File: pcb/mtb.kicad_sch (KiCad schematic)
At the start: 50 parts, among them J4 PINHEADER, J5 PROG/DEBUG, J6 PINHEADER, SW1 6x6, U12 STM32F103C8Tx, U13 AMS1117-3.3, U14 L78L05_SOT89, U15 SN75176AP, Y1 14,7456MHz

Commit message: Added Schottky in DCC part and fuse footprint.
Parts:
- F3: footprint (none) -> Fuse:Fuse_1812_4532Metric_Pad1.30x3.40mm_HandSolder
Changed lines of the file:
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@@
       (effects (font (size 1.27 1.27)))
     )
-    (property "Footprint" "" (at 265.43 26.67 0)
+    (property "Footprint" "Fuse:Fuse_1812_4532Metric_Pad1.30x3.40mm_HandSolder" (at 265.43 26.67 0)
       (effects (font (size 1.27 1.27)) (justify left) hide)
     )

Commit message: Add several notes.
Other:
- note added: "10k/each"
- moved on the sheet: D4, D5, D6, R39, R41, R42, SW1

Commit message: PCB WIP.
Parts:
- renumbered J4 to J7, J5 to J8
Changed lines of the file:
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@@
   (symbol (lib_id "Connector_Generic:Conn_02x05_Odd_Even") (at 74.93 176.53 0) (unit 1)
     (in_bom yes) (on_board yes) (dnp no)
-    (property "Reference" "J5" (at 76.2 165.9382 0)
+    (property "Reference" "J8" (at 76.2 165.9382 0)
       (effects (font (size 1.27 1.27)))
     )
@@
       (project "railcomdet"
         (path "/3e59d29f-2657-4552-9290-3c54fadfdf63/c65c8567-2dc1-4e1e-ba1a-da7bb38dcfe3"
-          (reference "J5") (unit 1)
+          (reference "J8") (unit 1)
         )
       )
@@
   (symbol (lib_id "Connector_Generic:Conn_01x02") (at 31.75 72.39 0) (mirror y) (unit 1)
     (in_bom yes) (on_board yes) (dnp no)
-    (property "Reference" "J4" (at 31.75 80.01 0)
+    (property "Reference" "J7" (at 31.75 80.01 0)
       (effects (font (size 1.27 1.27)))
     )
@@
       (project "railcomdet"
         (path "/3e59d29f-2657-4552-9290-3c54fadfdf63/c65c8567-2dc1-4e1e-ba1a-da7bb38dcfe3"
-          (reference "J4") (unit 1)
-        )
-      )
+          (reference "J7") (unit 1)
+        )
+      )

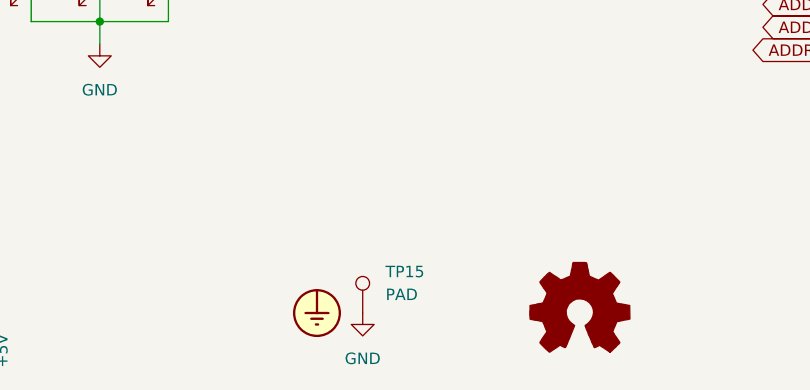
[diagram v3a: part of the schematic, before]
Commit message: pcb: wire multiplexer's inputs.
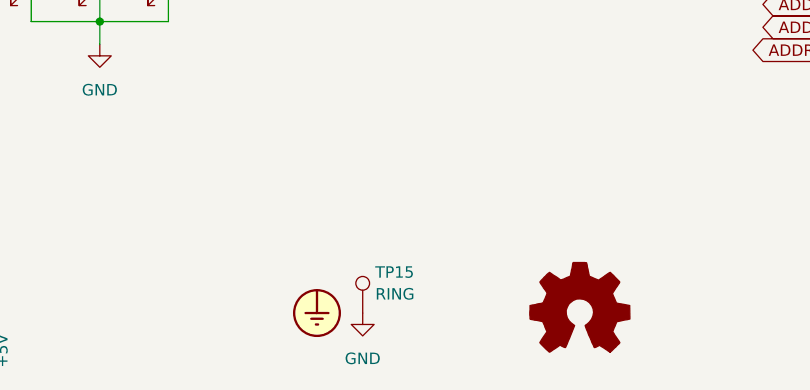
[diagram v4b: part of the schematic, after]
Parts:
- TP15: value PAD -> RING; footprint TestPoint:TestPoint_Pad_D2.0mm -> TestPoint:TestPoint_Loop_D1.80mm_Drill1.0mm_Beaded
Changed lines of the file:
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@@
   (symbol (lib_id "Connector:TestPoint") (at 142.24 181.61 0) (unit 1)
     (in_bom yes) (on_board yes) (dnp no) (fields_autoplaced)
-    (property "Reference" "TP15" (at 144.78 177.038 0)
+    (property "Reference" "TP15" (at 143.637 177.0959 0)
       (effects (font (size 1.27 1.27)) (justify left))
     )
-    (property "Value" "PAD" (at 144.78 179.578 0)
+    (property "Value" "RING" (at 143.637 179.5201 0)
       (effects (font (size 1.27 1.27)) (justify left))
     )
-    (property "Footprint" "TestPoint:TestPoint_Pad_D2.0mm" (at 147.32 181.61 0)
+    (property "Footprint" "TestPoint:TestPoint_Loop_D1.80mm_Drill1.0mm_Beaded" (at 147.32 181.61 0)
       (effects (font (size 1.27 1.27)) hide)
     )
@@
       (effects (font (size 1.27 1.27)) hide)
     )
+    (property "Field4" "" (at 142.24 181.61 0)
+      (effects (font (size 1.27 1.27)) hide)
+    )

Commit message: pcb: everything routed.
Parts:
- C24, C25, C26: footprint Capacitor_SMD:C_0805_2012Metric -> Capacitor_SMD:C_0805_2012Metric_Pad1.18x1.45mm_HandSolder
- JP1, JP2: footprint Jumper:SolderJumper-2_P1.3mm_Open_RoundedPad1.0x1.5mm -> Connector_PinHeader_2.54mm:PinHeader_1x02_P2.54mm_Vertical
- SW1: symbol Switch:SW_MEC_5E -> Switch:SW_Push
- TP16, TP17, TP18: footprint TestPoint:TestPoint_Pad_D2.0mm -> Connector_PinHeader_2.54mm:PinHeader_1x01_P2.54mm_Vertical
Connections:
- net GND: no longer SW1.2
- net MTB-TE: now also U15.3 (DE); no longer U15.4 (D)
- net MTB-TX: now also U15.4 (D); no longer U15.3 (DE)
- net at U12.28 (PB15): now also SW1.2; no longer SW1.4 (A)
- no-connect marks 13 -> 12
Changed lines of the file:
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@@
   (junction (at 175.26 27.94) (diameter 0) (color 0 0 0 0)
   )
-  (junction (at 92.71 142.24) (diameter 0) (color 0 0 0 0)
-  )
   (junction (at 254 134.62) (diameter 0) (color 0 0 0 0)
   )
-  (junction (at 206.375 86.36) (diameter 0) (color 0 0 0 0)
-  )
   (junction (at 241.3 139.7) (diameter 0) (color 0 0 0 0)
   )
@@
   (junction (at 233.68 53.34) (diameter 0) (color 0 0 0 0)
   )
+  (junction (at 206.375 88.9) (diameter 0) (color 0 0 0 0)
+  )
   (junction (at 241.3 39.37) (diameter 0) (color 0 0 0 0)
   )
@@
   (junction (at 247.65 88.9) (diameter 0) (color 0 0 0 0)
   )
-  (junction (at 229.87 86.36) (diameter 0) (color 0 0 0 0)
-  )
   (junction (at 113.03 149.225) (diameter 0) (color 0 0 0 0)
   )
@@
   (junction (at 212.09 120.65) (diameter 0) (color 0 0 0 0)
   )
-  (junction (at 200.66 81.28) (diameter 0) (color 0 0 0 0)
+  (junction (at 200.66 83.82) (diameter 0) (color 0 0 0 0)
   )
   (junction (at 234.95 120.65) (diameter 0) (color 0 0 0 0)
@@
   (no_connect (at 53.34 77.47))
   (no_connect (at 86.36 77.47))
-  (no_connect (at 92.71 132.08))
   (no_connect (at 53.34 82.55))
   (no_connect (at 86.36 80.01))
@@
     (stroke (width 0) (type default))
   )
+  (wire (pts (xy 200.66 83.82) (xy 231.14 83.82))
+    (stroke (width 0) (type default))
+  )
   (wire (pts (xy 270.51 144.78) (xy 270.51 147.32))
     (stroke (width 0) (type default))
@@
     (stroke (width 0) (type default))
   )
-  (wire (pts (xy 200.66 81.28) (xy 231.14 81.28))
-    (stroke (width 0) (type default))
-  )
   (wire (pts (xy 90.17 74.93) (xy 97.79 74.93))
     (stroke (width 0) (type default))
@@
     (stroke (width 0) (type default))
   )
-  (wire (pts (xy 95.25 125.73) (xy 95.25 132.08))
+  (wire (pts (xy 92.71 125.73) (xy 92.71 132.08))
     (stroke (width 0) (type default))
   )
@@
     (stroke (width 0) (type default))
   )
-  (wire (pts (xy 95.25 142.24) (xy 92.71 142.24))
-    (stroke (width 0) (type default))
-  )
   (wire (pts (xy 66.04 52.07) (xy 63.5 52.07))
     (stroke (width 0) (type default))
@@
     (stroke (width 0) (type default))
   )
-  (wire (pts (xy 206.375 86.36) (xy 229.87 86.36))
+  (wire (pts (xy 196.85 88.9) (xy 206.375 88.9))
     (stroke (width 0) (type default))
   )
@@
     (stroke (width 0) (type default))
   )
+  (wire (pts (xy 92.71 125.73) (xy 86.36 125.73))
+    (stroke (width 0) (type default))
+  )
   (wire (pts (xy 86.36 64.77) (xy 88.9 64.77))
     (stroke (width 0) (type default))
@@
     (stroke (width 0) (type default))
   )
-  (wire (pts (xy 95.25 125.73) (xy 86.36 125.73))
-    (stroke (width 0) (type default))
-  )
   (wire (pts (xy 205.74 125.73) (xy 205.74 120.65))
     (stroke (width 0) (type default))
@@
     (stroke (width 0) (type default))
   )
-  (wire (pts (xy 206.375 77.47) (xy 206.375 86.36))
+  (wire (pts (xy 206.375 77.47) (xy 206.375 88.9))
     (stroke (width 0) (type default))
   )
@@
     (stroke (width 0) (type default))
   )
-  (wire (pts (xy 231.14 83.82) (xy 229.87 83.82))
-    (stroke (width 0) (type default))
-  )
   (wire (pts (xy 64.77 25.4) (xy 54.61 25.4))
     (stroke (width 0) (type default))
@@
     (stroke (width 0) (type default))
   )
-  (wire (pts (xy 196.85 81.28) (xy 200.66 81.28))
+  (wire (pts (xy 196.85 83.82) (xy 200.66 83.82))
     (stroke (width 0) (type default))
   )
@@
     (stroke (width 0) (type default))
   )
-  (wire (pts (xy 229.87 86.36) (xy 229.87 88.9))
+  (wire (pts (xy 229.87 81.28) (xy 229.87 88.9))
     (stroke (width 0) (type default))
   )
@@
     (stroke (width 0) (type default))
   )
-  (wire (pts (xy 196.85 86.36) (xy 206.375 86.36))
-    (stroke (width 0) (type default))
-  )
   (wire (pts (xy 82.55 181.61) (xy 83.82 181.61))
     (stroke (width 0) (type default))
@@
     (stroke (width 0) (type default))
   )
-  (wire (pts (xy 229.87 83.82) (xy 229.87 86.36))
-    (stroke (width 0) (type default))
-  )
   (wire (pts (xy 105.41 146.685) (xy 105.41 149.225))
     (stroke (width 0) (type default))
@@
     (stroke (width 0) (type default))
   )
-  (wire (pts (xy 200.66 77.47) (xy 200.66 81.28))
+  (wire (pts (xy 200.66 77.47) (xy 200.66 83.82))
+    (stroke (width 0) (type default))
+  )
+  (wire (pts (xy 206.375 88.9) (xy 229.87 88.9))
     (stroke (width 0) (type default))
   )
@@
     (stroke (width 0) (type default))
   )
+  (wire (pts (xy 229.87 81.28) (xy 231.14 81.28))
+    (stroke (width 0) (type default))
+  )
   (wire (pts (xy 267.97 152.4) (xy 270.51 152.4))
     (stroke (width 0) (type default))
@@
     )
   )
-  (global_label "MTB-TE" (shape input) (at 196.85 86.36 180) (fields_autoplaced)
+  (global_label "MTB-TE" (shape input) (at 196.85 88.9 180) (fields_autoplaced)
     (effects (font (size 1.27 1.27)) (justify right))
-    (property "Intersheetrefs" "${INTERSHEET_REFS}" (at 186.4868 86.36 0)
+    (property "Intersheetrefs" "${INTERSHEET_REFS}" (at 186.4868 88.9 0)
       (effects (font (size 1.27 1.27)) (justify right) hide)
     )
@@
     )
   )
-  (global_label "MTB-TX" (shape input) (at 196.85 81.28 180) (fields_autoplaced)
+  (global_label "MTB-TX" (shape input) (at 196.85 83.82 180) (fields_autoplaced)
     (effects (font (size 1.27 1.27)) (justify right))
-    (property "Intersheetrefs" "${INTERSHEET_REFS}" (at 186.4263 81.28 0)
+    (property "Intersheetrefs" "${INTERSHEET_REFS}" (at 186.4263 83.82 0)
       (effects (font (size 1.27 1.27)) (justify right) hide)
     )
@@
       (effects (font (size 1.27 1.27)) (justify left) hide)
     )
-    (property "Footprint" "TestPoint:TestPoint_Pad_D2.0mm" (at 211.455 77.47 0)
+    (property "Footprint" "Connector_PinHeader_2.54mm:PinHeader_1x01_P2.54mm_Vertical" (at 211.455 77.47 0)
       (effects (font (size 1.27 1.27)) hide)
     )
@@
       (effects (font (size 1.27 1.27)))
     )
-    (property "Footprint" "Jumper:SolderJumper-2_P1.3mm_Open_RoundedPad1.0x1.5mm" (at 93.98 185.42 0)
+    (property "Footprint" "Connector_PinHeader_2.54mm:PinHeader_1x02_P2.54mm_Vertical" (at 93.98 185.42 0)
       (effects (font (size 1.27 1.27)) hide)
     )
@@
       (effects (font (size 1.27 1.27)) (justify left) hide)
     )
-    (property "Footprint" "TestPoint:TestPoint_Pad_D2.0mm" (at 205.74 77.47 0)
+    (property "Footprint" "Connector_PinHeader_2.54mm:PinHeader_1x01_P2.54mm_Vertical" (at 205.74 77.47 0)
       (effects (font (size 1.27 1.27)) hide)
     )
@@
       (effects (font (size 1.27 1.27)) (justify right))
     )
-    (property "Footprint" "Capacitor_SMD:C_0805_2012Metric" (at 214.3252 45.72 0)
+    (property "Footprint" "Capacitor_SMD:C_0805_2012Metric_Pad1.18x1.45mm_HandSolder" (at 214.3252 45.72 0)
       (effects (font (size 1.27 1.27)) hide)
     )
@@
       (effects (font (size 1.27 1.27)) (justify right))
     )
-    (property "Footprint" "Capacitor_SMD:C_0805_2012Metric" (at 176.2252 27.94 0)
+    (property "Footprint" "Capacitor_SMD:C_0805_2012Metric_Pad1.18x1.45mm_HandSolder" (at 176.2252 27.94 0)
       (effects (font (size 1.27 1.27)) hide)
     )
@@
       (effects (font (size 1.27 1.27)) (justify right))
     )
-    (property "Footprint" "Capacitor_SMD:C_0805_2012Metric" (at 174.9552 45.72 0)
+    (property "Footprint" "Capacitor_SMD:C_0805_2012Metric_Pad1.18x1.45mm_HandSolder" (at 174.9552 45.72 0)
       (effects (font (size 1.27 1.27)) hide)
     )
@@
       (effects (font (size 1.27 1.27)) (justify left) hide)
     )
-    (property "Footprint" "TestPoint:TestPoint_Pad_D2.0mm" (at 217.17 77.47 0)
+    (property "Footprint" "Connector_PinHeader_2.54mm:PinHeader_1x01_P2.54mm_Vertical" (at 217.17 77.47 0)
       (effects (font (size 1.27 1.27)) hide)
     )
@@
       (effects (font (size 1.27 1.27)))
     )
-    (property "Footprint" "Jumper:SolderJumper-2_P1.3mm_Open_RoundedPad1.0x1.5mm" (at 57.15 179.07 0)
+    (property "Footprint" "Connector_PinHeader_2.54mm:PinHeader_1x02_P2.54mm_Vertical" (at 57.15 179.07 0)
       (effects (font (size 1.27 1.27)) hide)
     )
@@
     )
   )
-  (symbol (lib_id "Switch:SW_MEC_5E") (at 92.71 137.16 270) (mirror x) (unit 1)
+  (symbol (lib_id "Switch:SW_Push") (at 92.71 137.16 270) (mirror x) (unit 1)
     (in_bom yes) (on_board yes) (dnp no)
     (property "Reference" "SW1" (at 88.265 137.16 0)
@@
       (effects (font (size 1.27 1.27)))
     )
-    (property "Footprint" "Button_Switch_THT:SW_PUSH_6mm_H4.3mm" (at 100.33 137.16 0)
+    (property "Footprint" "Button_Switch_THT:SW_PUSH_6mm_H4.3mm" (at 97.79 137.16 0)
       (effects (font (size 1.27 1.27)) hide)
     )
-    (property "Datasheet" "http://www.apem.com/int/index.php?controller=attachment&id_attachment=1371" (at 100.33 137.16 0)
+    (property "Datasheet" "~" (at 97.79 137.16 0)
       (effects (font (size 1.27 1.27)) hide)
     )
     (pin "1")
     (pin "2")
-    (pin "3")
-    (pin "4")
     (instances
       (project "railcomdet"

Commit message: Use handsolder SMDs where possible.
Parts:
- C17, C18, C19, C20, C22, C23, C27: footprint Capacitor_SMD:C_0805_2012Metric -> Capacitor_SMD:C_0805_2012Metric_Pad1.18x1.45mm_HandSolder
- D4, D5, D6: footprint LED_SMD:LED_0805_2012Metric -> LED_SMD:LED_0805_2012Metric_Pad1.15x1.40mm_HandSolder
- R39, R40, R41, R42, R43, R44, R45, R46, R47, R48, R49, R50, R51, R52: footprint Resistor_SMD:R_0805_2012Metric -> Resistor_SMD:R_0805_2012Metric_Pad1.20x1.40mm_HandSolder
- U14: footprint Package_TO_SOT_SMD:SOT-89-3 -> Package_TO_SOT_SMD:SOT-89-3_Handsoldering
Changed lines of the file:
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@@
       (effects (font (size 1.27 1.27)) (justify left) hide)
     )
-    (property "Footprint" "Resistor_SMD:R_0805_2012Metric" (at 252.222 129.54 90)
+    (property "Footprint" "Resistor_SMD:R_0805_2012Metric_Pad1.20x1.40mm_HandSolder" (at 252.222 129.54 90)
       (effects (font (size 1.27 1.27)) hide)
     )
@@
       (effects (font (size 1.27 1.27)) (justify left))
     )
-    (property "Footprint" "Resistor_SMD:R_0805_2012Metric" (at 114.808 132.715 90)
+    (property "Footprint" "Resistor_SMD:R_0805_2012Metric_Pad1.20x1.40mm_HandSolder" (at 114.808 132.715 90)
       (effects (font (size 1.27 1.27)) hide)
     )
@@
       (effects (font (size 1.27 1.27)) (justify left) hide)
     )
-    (property "Footprint" "Resistor_SMD:R_0805_2012Metric" (at 223.012 129.54 90)
+    (property "Footprint" "Resistor_SMD:R_0805_2012Metric_Pad1.20x1.40mm_HandSolder" (at 223.012 129.54 90)
       (effects (font (size 1.27 1.27)) hide)
     )
@@
       (effects (font (size 1.27 1.27)) (justify left) hide)
     )
-    (property "Footprint" "Resistor_SMD:R_0805_2012Metric" (at 216.662 129.54 90)
+    (property "Footprint" "Resistor_SMD:R_0805_2012Metric_Pad1.20x1.40mm_HandSolder" (at 216.662 129.54 90)
       (effects (font (size 1.27 1.27)) hide)
     )
@@
       (effects (font (size 1.27 1.27)) (justify left))
     )
-    (property "Footprint" "Resistor_SMD:R_0805_2012Metric" (at 239.522 46.99 90)
+    (property "Footprint" "Resistor_SMD:R_0805_2012Metric_Pad1.20x1.40mm_HandSolder" (at 239.522 46.99 90)
       (effects (font (size 1.27 1.27)) hide)
     )
@@
       (effects (font (size 1.27 1.27)) (justify right) hide)
     )
-    (property "Footprint" "Resistor_SMD:R_0805_2012Metric" (at 203.962 129.54 90)
+    (property "Footprint" "Resistor_SMD:R_0805_2012Metric_Pad1.20x1.40mm_HandSolder" (at 203.962 129.54 90)
       (effects (font (size 1.27 1.27)) hide)
     )
@@
       (effects (font (size 1.27 1.27)))
     )
-    (property "Footprint" "LED_SMD:LED_0805_2012Metric" (at 113.03 142.875 0)
+    (property "Footprint" "LED_SMD:LED_0805_2012Metric_Pad1.15x1.40mm_HandSolder" (at 113.03 142.875 0)
       (effects (font (size 1.27 1.27)) hide)
     )
@@
       (effects (font (size 1.27 1.27)))
     )
-    (property "Footprint" "LED_SMD:LED_0805_2012Metric" (at 120.65 142.875 0)
+    (property "Footprint" "LED_SMD:LED_0805_2012Metric_Pad1.15x1.40mm_HandSolder" (at 120.65 142.875 0)
       (effects (font (size 1.27 1.27)) hide)
     )
@@
       (effects (font (size 1.27 1.27)) (justify left) hide)
     )
-    (property "Footprint" "Resistor_SMD:R_0805_2012Metric" (at 245.872 129.54 90)
+    (property "Footprint" "Resistor_SMD:R_0805_2012Metric_Pad1.20x1.40mm_HandSolder" (at 245.872 129.54 90)
       (effects (font (size 1.27 1.27)) hide)
     )
@@
       (effects (font (size 1.27 1.27)))
     )
-    (property "Footprint" "Capacitor_SMD:C_0805_2012Metric" (at 227.33 75.8952 0)
+    (property "Footprint" "Capacitor_SMD:C_0805_2012Metric_Pad1.18x1.45mm_HandSolder" (at 227.33 75.8952 0)
       (effects (font (size 1.27 1.27)) hide)
     )
@@
       (effects (font (size 1.27 1.27)) (justify left))
     )
-    (property "Footprint" "Capacitor_SMD:C_0805_2012Metric" (at 53.6448 33.02 0)
+    (property "Footprint" "Capacitor_SMD:C_0805_2012Metric_Pad1.18x1.45mm_HandSolder" (at 53.6448 33.02 0)
       (effects (font (size 1.27 1.27)) hide)
     )
@@
       (effects (font (size 1.27 1.27)))
     )
-    (property "Footprint" "Resistor_SMD:R_0805_2012Metric" (at 92.71 66.548 90)
+    (property "Footprint" "Resistor_SMD:R_0805_2012Metric_Pad1.20x1.40mm_HandSolder" (at 92.71 66.548 90)
       (effects (font (size 1.27 1.27)) hide)
     )
@@
       (effects (font (size 1.27 1.27)) (justify left) hide)
     )
-    (property "Footprint" "Resistor_SMD:R_0805_2012Metric" (at 210.312 129.54 90)
+    (property "Footprint" "Resistor_SMD:R_0805_2012Metric_Pad1.20x1.40mm_HandSolder" (at 210.312 129.54 90)
       (effects (font (size 1.27 1.27)) hide)
     )
@@
       (effects (font (size 1.27 1.27)) (justify right) hide)
     )
-    (property "Footprint" "Resistor_SMD:R_0805_2012Metric" (at 233.172 129.54 90)
+    (property "Footprint" "Resistor_SMD:R_0805_2012Metric_Pad1.20x1.40mm_HandSolder" (at 233.172 129.54 90)
       (effects (font (size 1.27 1.27)) hide)
     )
@@
       (effects (font (size 1.27 1.27)))
     )
-    (property "Footprint" "Package_TO_SOT_SMD:SOT-89-3" (at 186.69 40.64 0)
+    (property "Footprint" "Package_TO_SOT_SMD:SOT-89-3_Handsoldering" (at 186.69 40.64 0)
       (effects (font (size 1.27 1.27) italic) hide)
     )
@@
       (effects (font (size 1.27 1.27)))
     )
-    (property "Footprint" "Capacitor_SMD:C_0805_2012Metric" (at 114.3 66.3448 0)
+    (property "Footprint" "Capacitor_SMD:C_0805_2012Metric_Pad1.18x1.45mm_HandSolder" (at 114.3 66.3448 0)
       (effects (font (size 1.27 1.27)) hide)
     )
@@
       (effects (font (size 1.27 1.27)) (justify left))
     )
-    (property "Footprint" "Capacitor_SMD:C_0805_2012Metric" (at 73.9648 33.02 0)
+    (property "Footprint" "Capacitor_SMD:C_0805_2012Metric_Pad1.18x1.45mm_HandSolder" (at 73.9648 33.02 0)
       (effects (font (size 1.27 1.27)) hide)
     )
@@
       (effects (font (size 1.27 1.27)) (justify left))
     )
-    (property "Footprint" "Capacitor_SMD:C_0805_2012Metric" (at 82.8548 33.02 0)
+    (property "Footprint" "Capacitor_SMD:C_0805_2012Metric_Pad1.18x1.45mm_HandSolder" (at 82.8548 33.02 0)
       (effects (font (size 1.27 1.27)) hide)
     )
@@
       (effects (font (size 1.27 1.27)) (justify left))
     )
-    (property "Footprint" "Resistor_SMD:R_0805_2012Metric" (at 107.188 132.715 90)
+    (property "Footprint" "Resistor_SMD:R_0805_2012Metric_Pad1.20x1.40mm_HandSolder" (at 107.188 132.715 90)
       (effects (font (size 1.27 1.27)) hide)
     )
@@
       (effects (font (size 1.27 1.27)) (justify left))
     )
-    (property "Footprint" "Capacitor_SMD:C_0805_2012Metric" (at 63.8048 33.02 0)
+    (property "Footprint" "Capacitor_SMD:C_0805_2012Metric_Pad1.18x1.45mm_HandSolder" (at 63.8048 33.02 0)
       (effects (font (size 1.27 1.27)) hide)
     )
@@
       (effects (font (size 1.27 1.27)) (justify left))
     )
-    (property "Footprint" "Resistor_SMD:R_0805_2012Metric" (at 122.428 132.715 90)
+    (property "Footprint" "Resistor_SMD:R_0805_2012Metric_Pad1.20x1.40mm_HandSolder" (at 122.428 132.715 90)
       (effects (font (size 1.27 1.27)) hide)
     )
@@
       (effects (font (size 1.27 1.27)))
     )
-    (property "Footprint" "LED_SMD:LED_0805_2012Metric" (at 105.41 142.875 0)
+    (property "Footprint" "LED_SMD:LED_0805_2012Metric_Pad1.15x1.40mm_HandSolder" (at 105.41 142.875 0)
       (effects (font (size 1.27 1.27)) hide)
     )
@@
       (effects (font (size 1.27 1.27)) (justify right))
     )
-    (property "Footprint" "Resistor_SMD:R_0805_2012Metric" (at 228.092 96.52 90)
+    (property "Footprint" "Resistor_SMD:R_0805_2012Metric_Pad1.20x1.40mm_HandSolder" (at 228.092 96.52 90)
       (effects (font (size 1.27 1.27)) hide)
     )
@@
       (effects (font (size 1.27 1.27)))
     )
-    (property "Footprint" "Capacitor_SMD:C_0805_2012Metric" (at 114.3 73.9648 0)
+    (property "Footprint" "Capacitor_SMD:C_0805_2012Metric_Pad1.18x1.45mm_HandSolder" (at 114.3 73.9648 0)
       (effects (font (size 1.27 1.27)) hide)
     )
@@
       (effects (font (size 1.27 1.27)) (justify left) hide)
     )
-    (property "Footprint" "Resistor_SMD:R_0805_2012Metric" (at 239.522 129.54 90)
-      (effects (font (size 1.27 1.27)) hide)
-    )
+    (property "Footprint" "Resistor_SMD:R_0805_2012Metric_Pad1.20x1.40mm_HandSolder" (at 239.522 129.54 90)
+      (effects (font (size 1.27 1.27)) hide)
+    )

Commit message: pcb: silkscreen.
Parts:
- C21: footprint Capacitor_SMD:C_0805_2012Metric -> Capacitor_SMD:C_0805_2012Metric_Pad1.18x1.45mm_HandSolder
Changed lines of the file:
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@@
       (effects (font (size 1.27 1.27)) (justify right))
     )
-    (property "Footprint" "Capacitor_SMD:C_0805_2012Metric" (at 93.0148 44.45 0)
+    (property "Footprint" "Capacitor_SMD:C_0805_2012Metric_Pad1.18x1.45mm_HandSolder" (at 93.0148 44.45 0)
       (effects (font (size 1.27 1.27)) hide)
     )
